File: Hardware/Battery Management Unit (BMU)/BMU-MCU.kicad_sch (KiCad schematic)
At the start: 9 parts, among them IC1 STM32C092RCT6, J13 Conn_ST_STDC14, SW2 RESET Switch

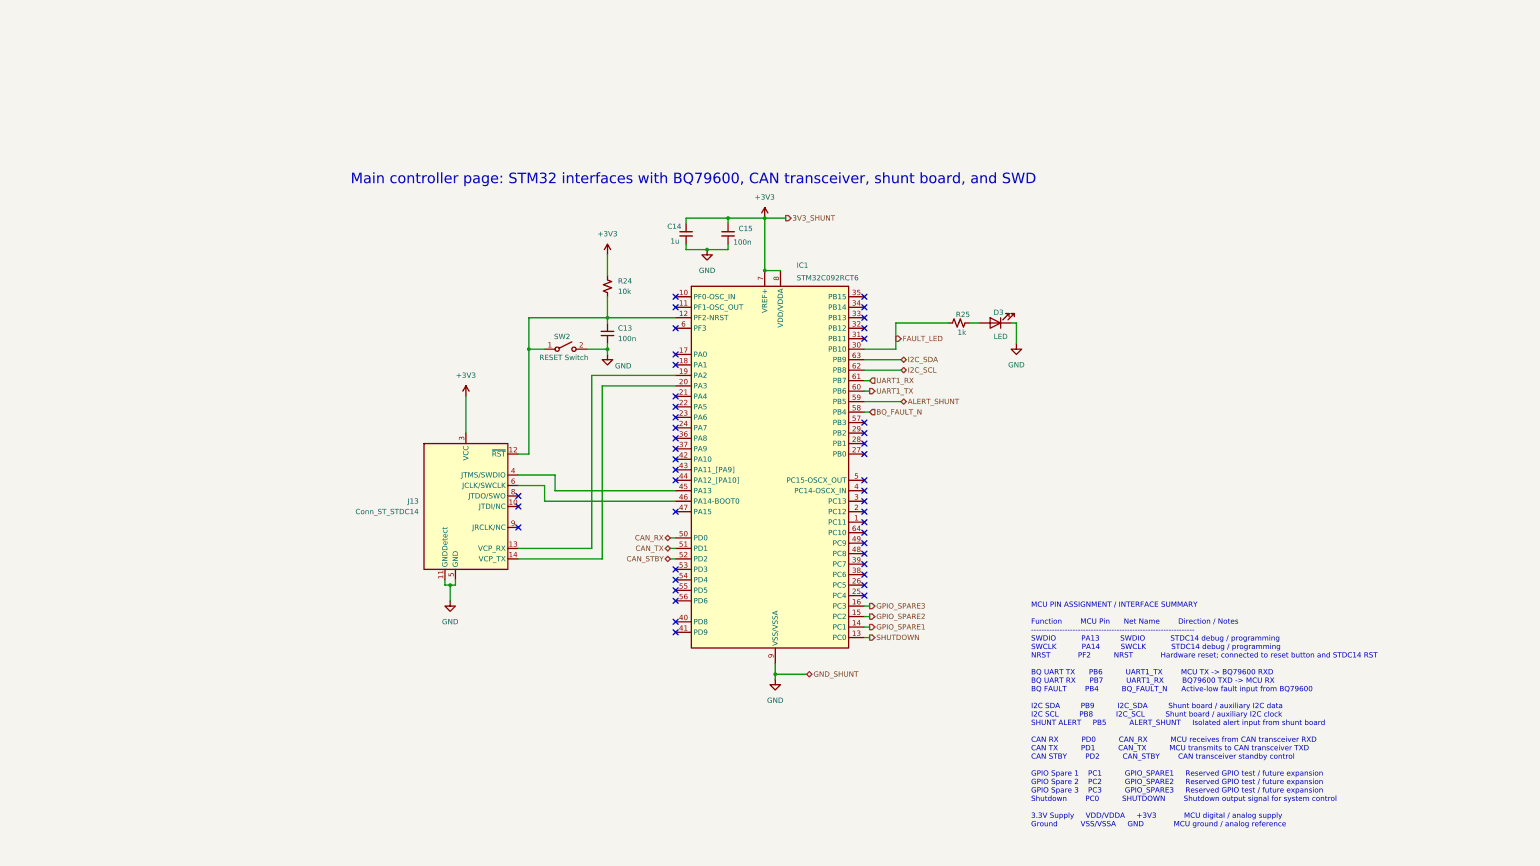
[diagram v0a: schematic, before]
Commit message: Schematic polish -- fixed to best standards, cleaned up for ERCs, etc
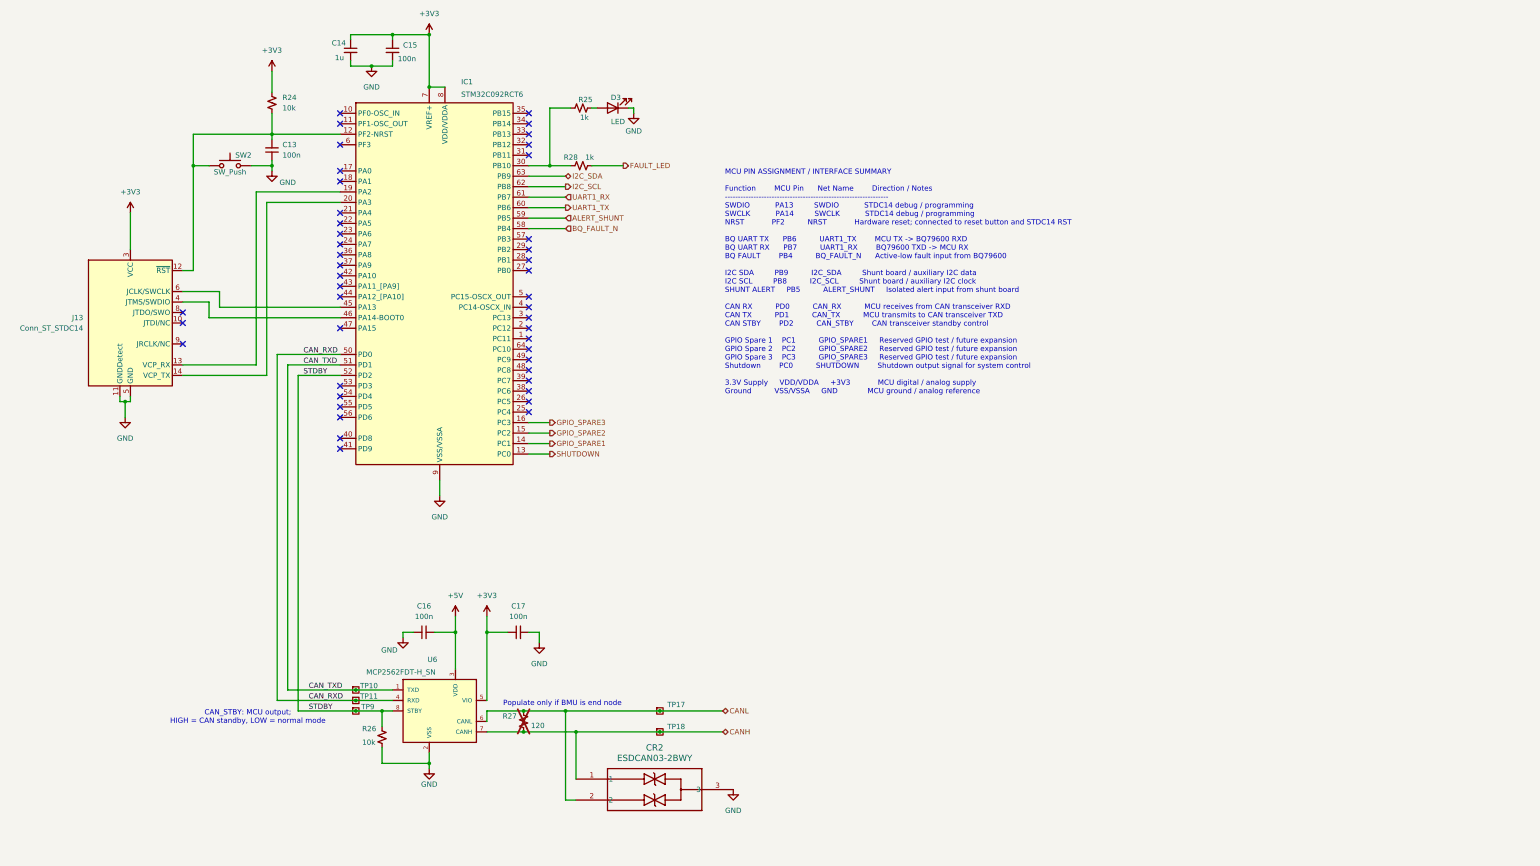
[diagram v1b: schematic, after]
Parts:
- added C16, C17: 100n, Capacitor_SMD:C_0805_2012Metric, symbol Device:C_Small
- added CR2: ESDCAN03-2BWY, ESDCAN03-2BWY:SOT323-3L_STM, symbol ESDCAN03-2BWY:ESDCAN03-2BWY
- added R26: 10k, Resistor_SMD:R_0805_2012Metric, symbol Device:R_Small_US
- added R27: 120, Resistor_SMD:R_0805_2012Metric, symbol Device:R_Small_US
- added R28: 1k, Resistor_SMD:R_0805_2012Metric, symbol Device:R_Small_US
- added TP10, TP11, TP17, TP18, TP9: TestPoint_Small, TestPoint:TestPoint_THTPad_D1.5mm_Drill0.7mm, symbol Connector:TestPoint_Square
- added U6: MCP2562FDT-H_SN, MCP2562FDT-H_SN:SOIC127P600X175-8N, symbol MCP2562FDT-H_SN:MCP2562FDT-H_SN
- SW2: value RESET Switch -> SW_Push; footprint Button_Switch_SMD:SW_Push_1P1T_NO_CK_KMR2 -> (none); symbol Switch:SW_SPST -> Switch:SW_Push
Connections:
- net +3V3: now also C17.1, U6.5 (VIO)
- net FAULT_LED: now also R28.2; no longer IC1.30 (PB10), R25.1
- net GND: now also J13.7 (GND), C16.1, C17.2, CR2.3, R26.2, U6.2 (VSS)
- net at IC1.45 (PA13): now also J13.6 (JCLK/SWCLK); no longer J13.4 (JTMS/SWDIO)
- net at IC1.46 (PA14-BOOT0): now also J13.4 (JTMS/SWDIO); no longer J13.6 (JCLK/SWCLK)
- net CAN_RX renamed CAN_RXD
- net CAN_RXD: now also TP11.1, U6.4 (RXD)
- net CAN_STBY renamed STDBY
- net STDBY: now also R26.1, TP9.1, U6.8 (STBY)
- net CAN_TX renamed CAN_TXD
- net CAN_TXD: now also TP10.1, U6.1 (TXD)
- new net: IC1.30 (PB10), R25.1, R28.1
- new net +5V: C16.2, U6.3 (VDD)
- new net CANH: CR2.1, R27.2, TP18.1, U6.7 (CANH)
- new net CANL: CR2.2, R27.1, TP17.1, U6.6 (CANL)
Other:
- note added: "CAN_STBY: MCU output; HIGH = CAN standby, LOW = normal mode"
- note added: "Populate only if BMU is end node"
- note removed: "Main controller page: STM32 interfaces with BQ79600, CAN transceiver, shunt board, and SWD"
- moved on the sheet: C13, C14, C15, D3, IC1, J13, R24, R25

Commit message: update libraries+bmu
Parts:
- CR2: footprint ESDCAN03-2BWY:SOT323-3L_STM -> Footprints:SOT323-3L_STM
- IC1: footprint STM32C092RCT6:QFP50P1200X1200X160-64N -> Footprints:QFP50P1200X1200X160-64N
- SW2: footprint (none) -> Button_Switch_THT:SW_PUSH_6mm_H4.3mm
- U6: footprint MCP2562FDT-H_SN:SOIC127P600X175-8N -> Footprints:SOIC127P600X175-8N
- renumbered J13 to J11, R26 to R25, R27 to R26, R25 to R27, TP10 to TP12, TP11 to TP13, TP9 to TP14, TP17 to TP15, TP18 to TP16
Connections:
- net at IC1.45 (PA13): now also J11.4 (JTMS/SWDIO); no longer J11.6 (JCLK/SWCLK)
- net at IC1.46 (PA14-BOOT0): now also J11.6 (JCLK/SWCLK); no longer J11.4 (JTMS/SWDIO)
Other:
- moved on the sheet: C13, C14, C15, C16, C17, CR2, D3, IC1, J11, R24, R25, R26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

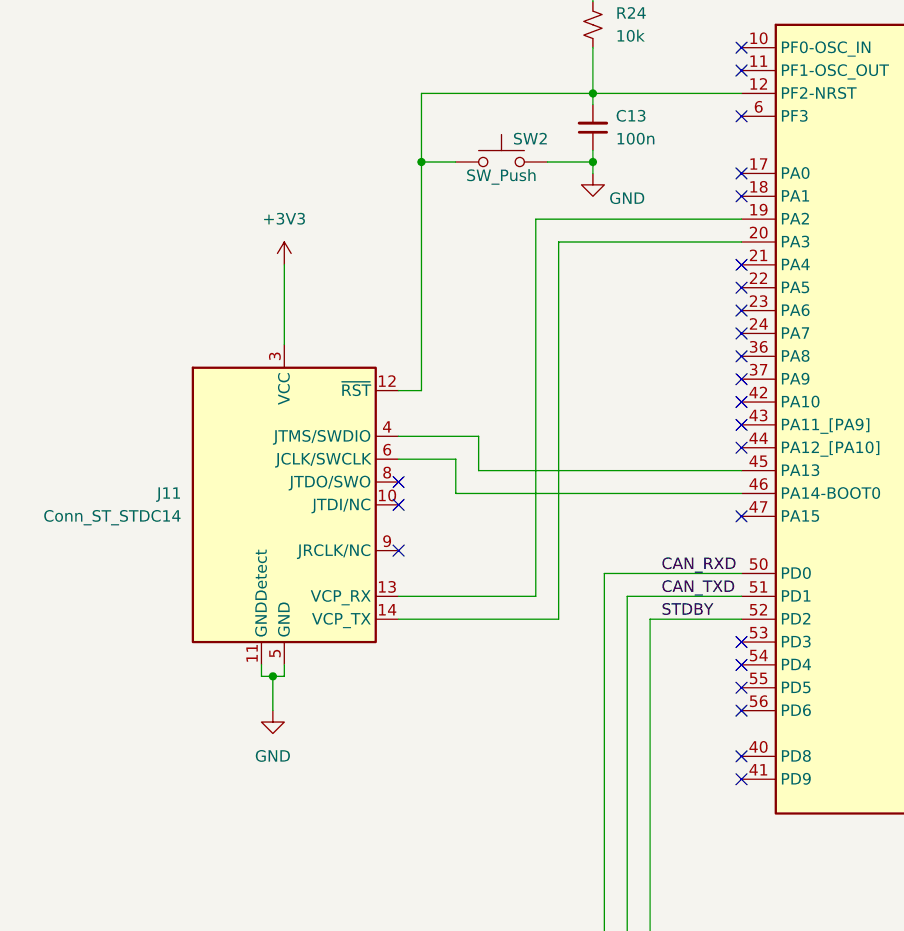
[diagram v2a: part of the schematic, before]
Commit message: Schematic cleanup; lots of missing library files
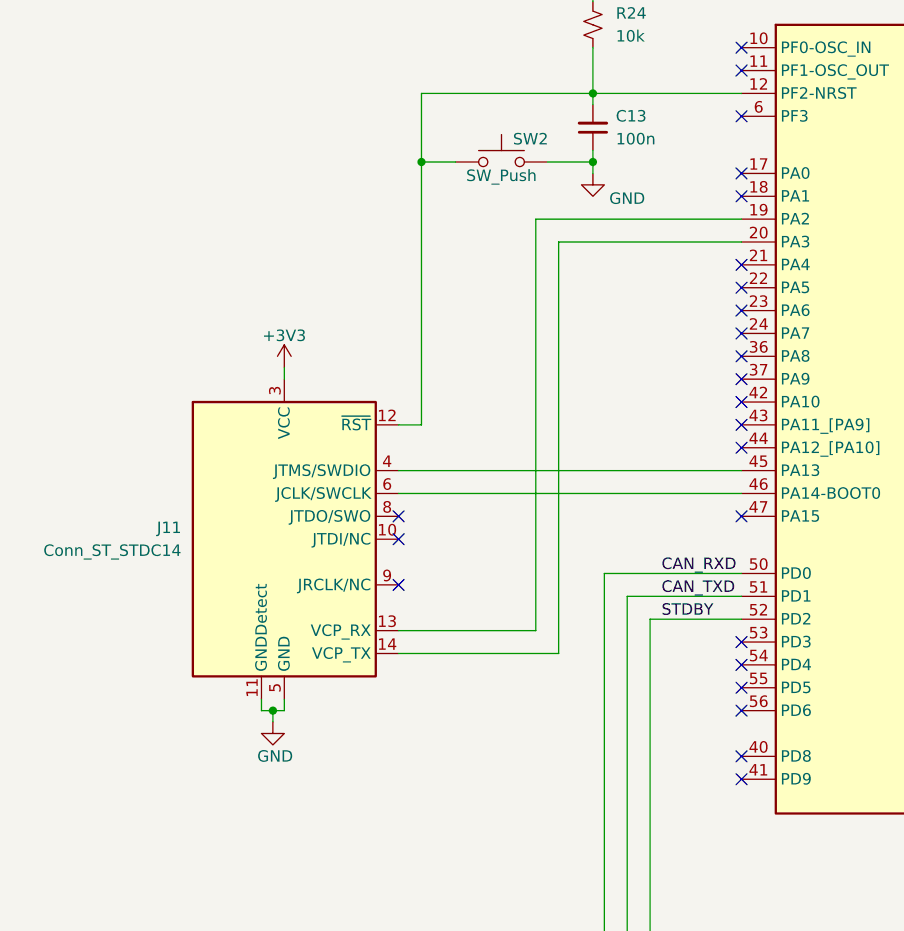
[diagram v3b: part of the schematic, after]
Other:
- moved on the sheet: J11
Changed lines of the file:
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@@
+	)
+	(junction
+		(at 109.22 142.24)
+		(diameter 0)
+		(color 0 0 0 0)
 	)
 	(junction
@@
 	)
 	(junction
-		(at 109.22 138.43)
-		(diameter 0)
-		(color 0 0 0 0)
-	)
-	(junction
 		(at 168.91 57.15)
 		(diameter 0)
@@
 	)
 	(no_connect
-		(at 123.19 124.46)
+		(at 123.19 128.27)
 	)
 	(no_connect
@@
 	)
 	(no_connect
-		(at 123.19 116.84)
+		(at 123.19 120.65)
 	)
 	(no_connect
@@
 	)
 	(no_connect
-		(at 123.19 119.38)
+		(at 123.19 123.19)
 	)
 	(no_connect
@@
 	(wire
 		(pts
-			(xy 138.43 87.63) (xy 138.43 129.54)
+			(xy 138.43 87.63) (xy 138.43 133.35)
 		)
 		(stroke
@@
 	(wire
 		(pts
-			(xy 129.54 118.11) (xy 161.29 118.11)
-		)
-		(stroke
-			(width 0)
-			(type default)
-		)
-	)
-	(wire
-		(pts
 			(xy 139.7 81.28) (xy 144.78 81.28)
 		)
@@
 	(wire
 		(pts
-			(xy 140.97 90.17) (xy 140.97 132.08)
+			(xy 140.97 90.17) (xy 140.97 135.89)
 		)
 		(stroke
@@
 	(wire
 		(pts
-			(xy 123.19 114.3) (xy 129.54 114.3)
+			(xy 123.19 118.11) (xy 161.29 118.11)
 		)
 		(stroke
@@
 	(wire
 		(pts
-			(xy 109.22 138.43) (xy 110.49 138.43)
+			(xy 109.22 142.24) (xy 110.49 142.24)
 		)
 		(stroke
@@
 	(wire
 		(pts
-			(xy 132.08 115.57) (xy 132.08 111.76)
-		)
-		(stroke
-			(width 0)
-			(type default)
-		)
-	)
-	(wire
-		(pts
-			(xy 110.49 137.16) (xy 110.49 138.43)
+			(xy 110.49 140.97) (xy 110.49 142.24)
 		)
 		(stroke
@@
 	(wire
 		(pts
-			(xy 132.08 115.57) (xy 161.29 115.57)
-		)
-		(stroke
-			(width 0)
-			(type default)
-		)
-	)
-	(wire
-		(pts
-			(xy 107.95 137.16) (xy 107.95 138.43)
+			(xy 107.95 140.97) (xy 107.95 142.24)
 		)
 		(stroke
@@
 	(wire
 		(pts
-			(xy 129.54 118.11) (xy 129.54 114.3)
-		)
-		(stroke
-			(width 0)
-			(type default)
-		)
-	)
-	(wire
-		(pts
 			(xy 173.99 57.15) (xy 173.99 55.88)
 		)
@@
 	(wire
 		(pts
-			(xy 125.73 81.28) (xy 125.73 106.68)
+			(xy 125.73 81.28) (xy 125.73 110.49)
 		)
 		(stroke
@@
 	(wire
 		(pts
-			(xy 123.19 129.54) (xy 138.43 129.54)
+			(xy 123.19 133.35) (xy 138.43 133.35)
 		)
 		(stroke
@@
 	(wire
 		(pts
-			(xy 110.49 92.71) (xy 110.49 101.6)
+			(xy 110.49 104.14) (xy 110.49 105.41)
 		)
 		(stroke
@@
 	(wire
 		(pts
-			(xy 109.22 138.43) (xy 109.22 142.24)
-		)
-		(stroke
-			(width 0)
-			(type default)
-		)
-	)
-	(wire
-		(pts
-			(xy 132.08 111.76) (xy 123.19 111.76)
-		)
-		(stroke
-			(width 0)
-			(type default)
-		)
-	)
-	(wire
-		(pts
-			(xy 140.97 132.08) (xy 123.19 132.08)
-		)
-		(stroke
-			(width 0)
-			(type default)
-		)
-	)
-	(wire
-		(pts
-			(xy 123.19 106.68) (xy 125.73 106.68)
-		)
-		(stroke
-			(width 0)
-			(type default)
-		)
-	)
-	(wire
-		(pts
-			(xy 107.95 138.43) (xy 109.22 138.43)
+			(xy 109.22 142.24) (xy 109.22 143.51)
+		)
+		(stroke
+			(width 0)
+			(type default)
+		)
+	)
+	(wire
+		(pts
+			(xy 123.19 115.57) (xy 161.29 115.57)
+		)
+		(stroke
+			(width 0)
+			(type default)
+		)
+	)
+	(wire
+		(pts
+			(xy 140.97 135.89) (xy 123.19 135.89)
+		)
+		(stroke
+			(width 0)
+			(type default)
+		)
+	)
+	(wire
+		(pts
+			(xy 123.19 110.49) (xy 125.73 110.49)
+		)
+		(stroke
+			(width 0)
+			(type default)
+		)
+	)
+	(wire
+		(pts
+			(xy 107.95 142.24) (xy 109.22 142.24)
 		)
 		(stroke
@@
 	(symbol
 		(lib_id "power:+3V3")
-		(at 110.49 92.71 0)
+		(at 110.49 104.14 0)
 		(unit 1)
 		(body_style 1)
@@
 		(in_pos_files yes)
 		(dnp no)
-		(fields_autoplaced yes)
 		(property "Reference" "#PWR035"
-			(at 110.49 96.52 0)
+			(at 110.49 107.95 0)
 			(hide yes)
 			(show_name no)
@@
 		)
 		(property "Value" "+3V3"
-			(at 110.49 87.63 0)
+			(at 110.49 100.584 0)
 			(show_name no)
 			(do_not_autoplace no)
@@
 		)
 		(property "Footprint" ""
-			(at 110.49 92.71 0)
+			(at 110.49 104.14 0)
 			(hide yes)
 			(show_name no)
@@
 		)
 		(property "Datasheet" ""
-			(at 110.49 92.71 0)
+			(at 110.49 104.14 0)
 			(hide yes)
 			(show_name no)
@@
 		)
 		(property "Description" "Power symbol creates a global label with name \"+3V3\""
-			(at 110.49 92.71 0)
+			(at 110.49 104.14 0)
 			(hide yes)
 			(show_name no)
@@
 	(symbol
 		(lib_id "power:GND")
-		(at 109.22 142.24 0)
+		(at 109.22 143.51 0)
 		(unit 1)
 		(body_style 1)
@@
 		(in_pos_files yes)
 		(dnp no)
-		(fields_autoplaced yes)
 		(property "Reference" "#PWR034"
-			(at 109.22 148.59 0)
+			(at 109.22 149.86 0)
 			(hide yes)
 			(show_name no)
@@
 		)
 		(property "Value" "GND"
-			(at 109.22 147.32 0)
+			(at 109.474 147.32 0)
 			(show_name no)
 			(do_not_autoplace no)
@@
 		)
 		(property "Footprint" ""
-			(at 109.22 142.24 0)
+			(at 109.22 143.51 0)
 			(hide yes)
 			(show_name no)
@@
 		)
 		(property "Datasheet" ""
-			(at 109.22 142.24 0)
+			(at 109.22 143.51 0)
 			(hide yes)
 			(show_name no)
@@
 		)
 		(property "Description" "Power symbol creates a global label with name \"GND\" , ground"
-			(at 109.22 142.24 0)
+			(at 109.22 143.51 0)
 			(hide yes)
 			(show_name no)
@@
 	(symbol
 		(lib_id "Connector:Conn_ST_STDC14")
-		(at 110.49 119.38 0)
+		(at 110.49 123.19 0)
 		(unit 1)
 		(body_style 1)
@@
 		(fields_autoplaced yes)
 		(property "Reference" "J11"
-			(at 99.06 118.1099 0)
+			(at 99.06 121.9199 0)
 			(show_name no)
 			(do_not_autoplace no)
@@
 		)
 		(property "Value" "Conn_ST_STDC14"
-			(at 99.06 120.6499 0)
+			(at 99.06 124.4599 0)
 			(show_name no)
 			(do_not_autoplace no)
@@
 		)
 		(property "Footprint" "Connector_PinHeader_1.27mm:PinHeader_2x07_P1.27mm_Vertical"
-			(at 110.49 119.38 0)
+			(at 110.49 123.19 0)
 			(hide yes)
 			(show_name no)
@@
 		)
 		(property "Datasheet" "https://www.st.com/content/ccc/resource/technical/document/user_manual/group1/99/49/91/b6/b2/3a/46/e5/DM00526767/files/DM00526767.pdf/jcr:content/translations/en.DM00526767.pdf"
-			(at 101.6 151.13 90)
+			(at 101.6 154.94 90)
 			(hide yes)
 			(show_name no)
@@
 		)
 		(property "Description" "ST Debug Connector, standard ARM Cortex-M SWD and JTAG interface plus UART"
-			(at 110.49 119.38 0)
-			(hide yes)
-			(show_name no)
+			(at 110.49 123.19 0)
+			(hide yes)
+			(show_name no)

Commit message: finish! update bmu layout+BOM
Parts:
- C13, C15, C16, C17: DIS (none) -> DigiKey; DPN (none) -> 311-1140-1-ND; MFR (none) -> YAGEO; MPN (none) -> CC0805KRX7R9BB104; Purchase Link (none) -> https://www.digikey.com/en/products/detail/yageo/CC0805KRX7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
- C14: DIS (none) -> DigiKey; DPN (none) -> 311-1365-1-ND; MFR (none) -> YAGEO; MPN (none) -> CC0805KKX7R7BB105; Purchase Link (none) -> https://www.digikey.com/en/products/detail/yageo/CC0805KKX7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
- CR2: DIS (none) -> DigiKey; DPN (none) -> 497-15846-1-ND; MFR (none) -> STMicroelectronics; MPN (none) -> ESDCAN03-2BWY; Purchase Link (none) -> https://www.digikey.com/en/products/detail/stmicroelectroni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
- D3: DIS (none) -> DigiKey; DPN (none) -> 160-1415-1-ND; MFR (none) -> Lite-On Inc.; MPN (none) -> LTST-C170KRKT; Purchase Link (none) -> https://www.digikey.com/en/products/detail/liteon/LTST-C170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
- IC1: DIS (none) -> DigiKey; DPN (none) -> 497-STM32C092RCT6-ND; MFR (none) -> STMicroelectronics; MPN (none) -> STM32C092RCT6; Purchase Link (none) -> https://www.digikey.com/en/products/detail/stmicroelectroni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
- J11: DIS (none) -> DigiKey; DPN (none) -> 612-FTSH-107-01-F-DV-K-ND; MFR (none) -> Samtec Inc.; MPN (none) -> FTSH-107-01-F-DV-K; Purchase Link (none) -> https://www.digikey.com/en/products/detail/samtec-inc/FTSH-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
- R24, R25: DIS (none) -> DigiKey; DPN (none) -> 311-10.0KCRCT-ND; MFR (none) -> YAGEO; MPN (none) -> RC0805FR-0710KL; Purchase Link (none) -> https://www.digikey.com/en/products/detail/yageo/RC0805FR-0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
- R26: DIS (none) -> DigiKey; DPN (none) -> 311-120CRCT-ND; MFR (none) -> YAGEO; MPN (none) -> RC0805FR-07120RL; Purchase Link (none) -> https://www.digikey.com/en/products/detail/yageo/RC0805FR-0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
- R27, R28: DIS (none) -> DigiKey; DPN (none) -> 311-1.00KCRCT-ND; MFR (none) -> YAGEO; MPN (none) -> RC0805FR-071KL; Purchase Link (none) -> https://www.digikey.com/en/products/detail/yageo/RC0805FR-0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
- SW2: DIS (none) -> DigiKey; DPN (none) -> SW400-ND; MFR (none) -> Omron Electronics Inc-EMC Div; MPN (none) -> B3F-1000; Purchase Link (none) -> https://www.digikey.com/en/products/detail/omron-electronic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
- U6: DIS (none) -> DigiKey; DPN (none) -> 150-MCP2562FDT-H/SNCT-ND; MFR (none) -> Microchip Technology; MPN (none) -> MCP2562FDT-H/SN; Purchase Link (none) -> https://www.digikey.com/en/products/detail/microchip-techno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

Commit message: Polishing, BOM fixes, stitching
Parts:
- TP12, TP13, TP14, TP15, TP16: now left out of the parts list
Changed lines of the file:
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@@
 	(title_block
 		(title "BATTERY MANAGEMENT UNIT (BMU)")
-		(date "2026-04-06")
+		(date "2026-06-02")
 		(rev "1.0")
 		(company "VIKING MOTOR SPORTS (VMS)")
@@
 		(body_style 1)
 		(exclude_from_sim no)
-		(in_bom yes)
+		(in_bom no)
 		(on_board yes)
 		(in_pos_files yes)
@@
 		(body_style 1)
 		(exclude_from_sim no)
-		(in_bom yes)
+		(in_bom no)
 		(on_board yes)
 		(in_pos_files yes)
@@
 		(body_style 1)
 		(exclude_from_sim no)
-		(in_bom yes)
+		(in_bom no)
 		(on_board yes)
 		(in_pos_files yes)
@@
 		(body_style 1)
 		(exclude_from_sim no)
-		(in_bom yes)
+		(in_bom no)
 		(on_board yes)
 		(in_pos_files yes)
@@
 		(body_style 1)
 		(exclude_from_sim no)
-		(in_bom yes)
+		(in_bom no)
 		(on_board yes)
 		(in_pos_files yes)
